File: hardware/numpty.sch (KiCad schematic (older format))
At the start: 46 parts, among them U2 MP3202

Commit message: Rev_0 schematic finished, first pass at PCB layout (no traces yet).
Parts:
- added C1: 4.7uF, Capacitor_SMD:C_1206_3216Metric_Pad1.42x1.75mm_HandSolder, symbol Device:C
- added C2: 2.2uF, Capacitor_SMD:C_1206_3216Metric_Pad1.42x1.75mm_HandSolder, symbol Device:C
- added C3: 10uF, Capacitor_SMD:C_1206_3216Metric_Pad1.42x1.75mm_HandSolder, symbol Device:C
- added C4, C5: 22pF, Capacitor_SMD:C_1206_3216Metric_Pad1.42x1.75mm_HandSolder, symbol Device:C
- added C6: 1uF, Capacitor_SMD:C_1206_3216Metric_Pad1.42x1.75mm_HandSolder, symbol Device:C
- added D1: 30V_500mA_Schottky, Diode_SMD:D_SOD-123, symbol Device:D_Schottky
- added J2: AVR-ISP, Connector_IDC:IDC-Header_2x03_P2.54mm_Vertical, symbol Connector:AVR-ISP-6
- added L1: 10uH, numpty:SRN3010TA, symbol Device:L
- added R1: 100k, Resistor_SMD:R_1206_3216Metric_Pad1.42x1.75mm_HandSolder, symbol Device:R
- added R2: 1.8, Resistor_SMD:R_1206_3216Metric_Pad1.42x1.75mm_HandSolder, symbol Device:R
- added R3, R4: 5k1, Resistor_SMD:R_1206_3216Metric_Pad1.42x1.75mm_HandSolder, symbol Device:R
- added R5, R6: 22, Resistor_SMD:R_1206_3216Metric_Pad1.42x1.75mm_HandSolder, symbol Device:R
- added R7: 10k, Resistor_SMD:R_1206_3216Metric_Pad1.42x1.75mm_HandSolder, symbol Device:R
- added R8: 300, Resistor_SMD:R_1206_3216Metric_Pad1.42x1.75mm_HandSolder, symbol Device:R
- added Y1: 16MHz, Crystal:Crystal_SMD_HC49-SD, symbol Device:Crystal
- D_0, D_1, D_2, D_3, D_4, D_5, D_6, D_7, D_8, D_9, D_M0, D_M1, D_M2, D_M3: footprint (none) -> Diode_SMD:D_SOD-123
- D_DIV0: renamed from D_/; footprint (none) -> Diode_SMD:D_SOD-123
- D_ENT0: renamed from D_ENT; footprint (none) -> Diode_SMD:D_SOD-123
- D_MIN0: renamed from D_-; footprint (none) -> Diode_SMD:D_SOD-123
- D_MUL0: renamed from D_*; footprint (none) -> Diode_SMD:D_SOD-123
- D_NL0: renamed from D_NL; footprint (none) -> Diode_SMD:D_SOD-123
- D_PER0: renamed from D_.; footprint (none) -> Diode_SMD:D_SOD-123
- D_PLU0: renamed from D_+; footprint (none) -> Diode_SMD:D_SOD-123
- J1: renamed from J?; footprint (none) -> Connector_USB:USB_C_Receptacle_GCT_USB4085
- LED_NUMLOCK0: renamed from D_NL_I; footprint (none) -> LED_SMD:LED_Cree-XQ_HandSoldering
- SW_0, SW_1, SW_2, SW_3, SW_4, SW_5, SW_6, SW_7, SW_8, SW_9, SW_M0, SW_M1, SW_M2, SW_M3: footprint (none) -> numpty:Gateron_LED_1.00u_Plate
- SW_DIV0: renamed from SW_/; footprint (none) -> numpty:Gateron_LED_1.00u_Plate
- SW_ENT0: renamed from SW_ENT; footprint (none) -> numpty:Gateron_LED_1.00u_Plate
- SW_MIN0: renamed from SW_-; footprint (none) -> numpty:Gateron_LED_1.00u_Plate
- SW_MUL0: renamed from SW_*; footprint (none) -> numpty:Gateron_LED_1.00u_Plate
- SW_NL0: renamed from SW_NL; footprint (none) -> numpty:Gateron_LED_1.00u_Plate
- SW_PER0: renamed from SW_.; footprint (none) -> numpty:Gateron_LED_1.00u_Plate
- SW_PLU0: renamed from SW_+; footprint (none) -> numpty:Gateron_LED_1.00u_Plate
- U2: footprint (none) -> Package_TO_SOT_SMD:TSOT-23-6_HandSoldering
- gave numbers to parts that had none: 1
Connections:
- net COL0: now also U1.41 (PF0)
- net COL1: now also U1.40 (PF1)
- net COL2: now also U1.39 (PF4)
- net COL3: now also U1.38 (PF5)
- net LEDS_ANODE: now also U2.5 (OV), C2.1, D1.1 (K)
- net LEDS_CATHODE: now also U2.3 (FB), R2.1
- net ROW0: now also U1.18 (PD0)
- net ROW1: now also U1.19 (PD1)
- net ROW2: now also U1.20 (PD2)
- net ROW3: now also U1.21 (PD3)
- net ROW4: now also U1.25 (PD4)
- net ROW5: now also U1.22 (PD5)
- net GND: now reaches J1.A1 (GND)
- net GND: now also J1.A12 (GND), J1.B1 (GND), J1.B12 (GND), LED_NUMLOCK0.2 (A), U1.15 (GND), U1.23 (GND), U1.35 (GND), U1.43 (GND), U1.5 (UGND), U2.2 (GND), C1.2, C2.2, C3.2, C4.2, C5.2, C6.1, J2.6 (GND), R1.2, R2.2, R3.1, R4.1
- net +5V: now reaches J1.A4 (VBUS)
- net +5V: now also J1.A9 (VBUS), J1.B4 (VBUS), J1.B9 (VBUS), U1.14 (VCC), U1.2 (UVCC), U1.24 (AVCC), U1.34 (VCC), U1.44 (AVCC), U1.7 (VBUS), U2.6 (IN), C1.1, C3.1, J2.2 (VCC), L1.1, R7.1
- net at J1.A5 (CC1): now also R3.2
- net at J1.A6 (D+): now also J1.B6 (D+), R6.2
- net at J1.A7 (D-): now also J1.B7 (D-), R5.2
- net at J1.B5 (CC2): now also R4.2
- net at U2.1 (SW): now also D1.2 (A), L1.2
- net LEDS_PWM: now reaches U2.4 (EN)
- net LEDS_PWM: now also U1.32 (PC7), R1.1
- net MOSI: now reaches U1.10 (PB2)
- net MOSI: now also J2.4 (MOSI)
- net MISO: now reaches U1.11 (PB3)
- net MISO: now also J2.1 (MISO)
- net !RESET: now reaches U1.13 (~RESET)
- net !RESET: now also J2.5 (~RST), R7.2
- net at U1.16 (XTAL2): now also C5.1, Y1.2
- net at U1.17 (XTAL1): now also C4.1, Y1.1
- net D-: now reaches U1.3 (D-)
- net D-: now also R5.1
- net at U1.31 (PC6): now also R8.2
- net D+: now reaches U1.4 (D+)
- net D+: now also R6.1
- net at U1.6 (UCAP): now also C6.2
- net SCK: now reaches U1.9 (PB1)
- net SCK: now also J2.3 (SCK)
- net at LED_NUMLOCK0.1 (K): now also R8.1
- no-connect marks 0 -> 15
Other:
- note added: "20210308"
- note added: "numpty"
- moved on the sheet: D_0, D_1, D_2, D_3, D_4, D_5, D_6, D_7, D_8, D_9, D_DIV0, D_ENT0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

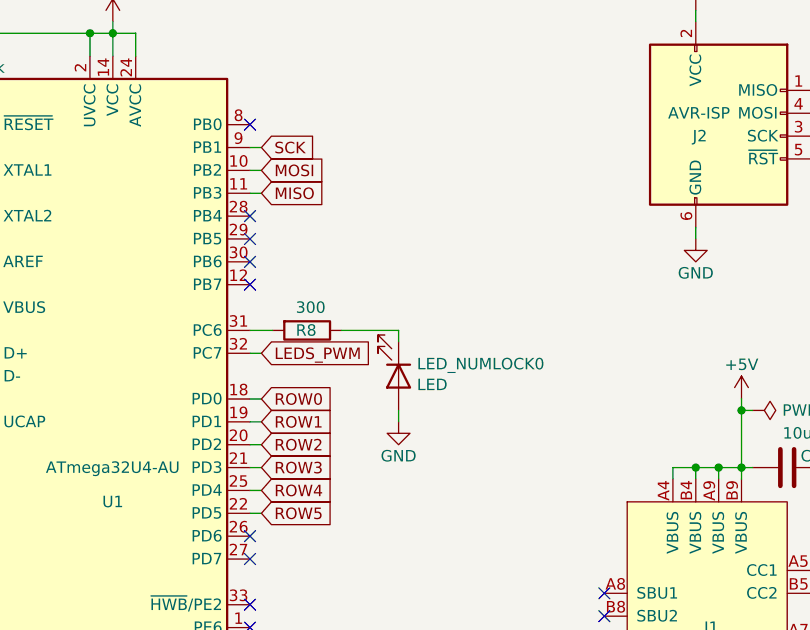
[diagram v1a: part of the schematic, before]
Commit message: Moved led pins to port B.  Added push-button on port B.  Reworked layout to suit these changes.
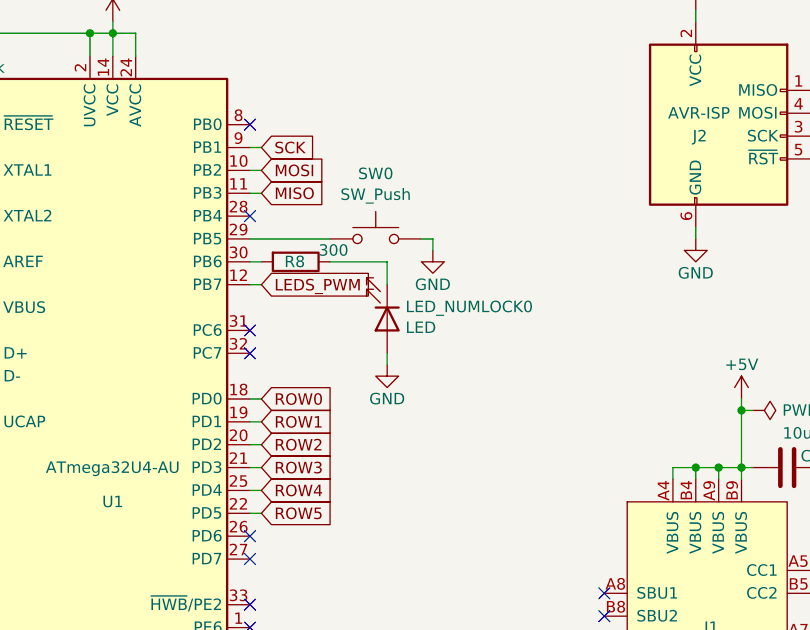
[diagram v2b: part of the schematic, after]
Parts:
- added SW0: SW_Push, Button_Switch_SMD:SW_Push_1P1T_NO_6x6mm_H9.5mm, symbol Switch:SW_Push
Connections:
- net GND: now also SW0.2
- net LEDS_PWM: now also U1.12 (PB7); no longer U1.32 (PC7)
- net at U1.29 (PB5): now also SW0.1
- net at U1.30 (PB6): now also R8.2
- net at U1.31 (PC6): no longer R8.2
- no-connect marks 15 -> 14
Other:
- moved on the sheet: LED_NUMLOCK0, R8
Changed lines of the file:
@@
 L Device:LED LED_NUMLOCK0
 U 1 1 60849E17
-P 8050 2450
-F 0 "LED_NUMLOCK0" V 7997 2530 50  0000 L CNN
-F 1 "LED" V 8088 2530 50  0000 L CNN
-F 2 "LED_SMD:LED_Cree-XQ_HandSoldering" H 8050 2450 50  0001 C CNN
-F 3 "~" H 8050 2450 50  0001 C CNN
-	1    8050 2450
+P 8000 2200
+F 0 "LED_NUMLOCK0" V 7947 2280 50  0000 L CNN
+F 1 "LED" V 8038 2280 50  0000 L CNN
+F 2 "LED_SMD:LED_Cree-XQ_HandSoldering" H 8000 2200 50  0001 C CNN
+F 3 "~" H 8000 2200 50  0001 C CNN
+	1    8000 2200
 	0    1    1    0
 $EndComp
@@
 L Device:R R8
 U 1 1 60C3E138
-P 7650 2250
-F 0 "R8" V 7650 2200 50  0000 L CNN
-F 1 "300" V 7550 2200 50  0000 L CNN
-F 2 "Resistor_SMD:R_1206_3216Metric_Pad1.42x1.75mm_HandSolder" V 7580 2250 50  0001 C CNN
-F 3 "~" H 7650 2250 50  0001 C CNN
-	1    7650 2250
+P 7600 1950
+F 0 "R8" V 7600 1900 50  0000 L CNN
+F 1 "300" V 7550 2050 50  0000 L CNN
+F 2 "Resistor_SMD:R_1206_3216Metric_Pad1.42x1.75mm_HandSolder" V 7530 1950 50  0001 C CNN
+F 3 "~" H 7600 1950 50  0001 C CNN
+	1    7600 1950
 	0    1    1    0
 $EndComp
@@
 Wire Wire Line
 	9350 900  9350 850
-Text GLabel 7450 2350 2    50   Input ~ 0
+Text GLabel 7450 2050 2    50   Input ~ 0
 LEDS_PWM
 Text GLabel 7450 2550 2    50   Input ~ 0
@@
 Text GLabel 7450 4050 2    50   Input ~ 0
 COL3
-Wire Wire Line
-	7400 2250 7500 2250
-Wire Wire Line
-	7800 2250 8050 2250
-Wire Wire Line
-	8050 2250 8050 2300
 $Comp
 L power:GND #PWR0115
 U 1 1 60F7D3CB
-P 8050 2650
-F 0 "#PWR0115" H 8050 2400 50  0001 C CNN
-F 1 "GND" H 8050 2500 50  0000 C CNN
-F 2 "" H 8050 2650 50  0001 C CNN
-F 3 "" H 8050 2650 50  0001 C CNN
-	1    8050 2650
-	1    0    0    -1
-$EndComp
-Wire Wire Line
-	8050 2650 8050 2600
-Wire Wire Line
-	7450 2350 7400 2350
+P 8000 2400
+F 0 "#PWR0115" H 8000 2150 50  0001 C CNN
+F 1 "GND" H 8000 2250 50  0000 C CNN
+F 2 "" H 8000 2400 50  0001 C CNN
+F 3 "" H 8000 2400 50  0001 C CNN
+	1    8000 2400
+	1    0    0    -1
+$EndComp
 Wire Wire Line
 	7400 2550 7450 2550
@@
 NoConn ~ 7400 1750
 NoConn ~ 7400 1350
-NoConn ~ 7400 1850
-NoConn ~ 7400 1950
-NoConn ~ 7400 2050
 NoConn ~ 7400 3150
 NoConn ~ 7400 3250
@@
 	1    0    0    -1
 $EndComp
+Wire Wire Line
+	7450 1950 7400 1950
+Wire Wire Line
+	7400 2050 7450 2050
+Wire Wire Line
+	8000 1950 7750 1950
+NoConn ~ 7400 2350
+NoConn ~ 7400 2250
+$Comp
+L Switch:SW_Push SW0
+U 1 1 605D1A0D
+P 7950 1850
+F 0 "SW0" H 7950 2135 50  0000 C CNN
+F 1 "SW_Push" H 7950 2044 50  0000 C CNN
+F 2 "Button_Switch_SMD:SW_Push_1P1T_NO_6x6mm_H9.5mm" H 7950 2050 50  0001 C CNN
+F 3 "~" H 7950 2050 50  0001 C CNN
+	1    7950 1850
+	1    0    0    -1
+$EndComp
+Wire Wire Line
+	7400 1850 7750 1850
+$Comp
+L power:GND #PWR0116
+U 1 1 605EDB5F
+P 8200 1900
+F 0 "#PWR0116" H 8200 1650 50  0001 C CNN
+F 1 "GND" H 8200 1750 50  0000 C CNN
+F 2 "" H 8200 1900 50  0001 C CNN
+F 3 "" H 8200 1900 50  0001 C CNN
+	1    8200 1900
+	1    0    0    -1
+$EndComp
+Wire Wire Line
+	8150 1850 8200 1850
+Wire Wire Line
+	8200 1850 8200 1900
+Wire Wire Line
+	8000 1950 8000 2050
+Wire Wire Line
+	8000 2350 8000 2400
 $EndSCHEMATC

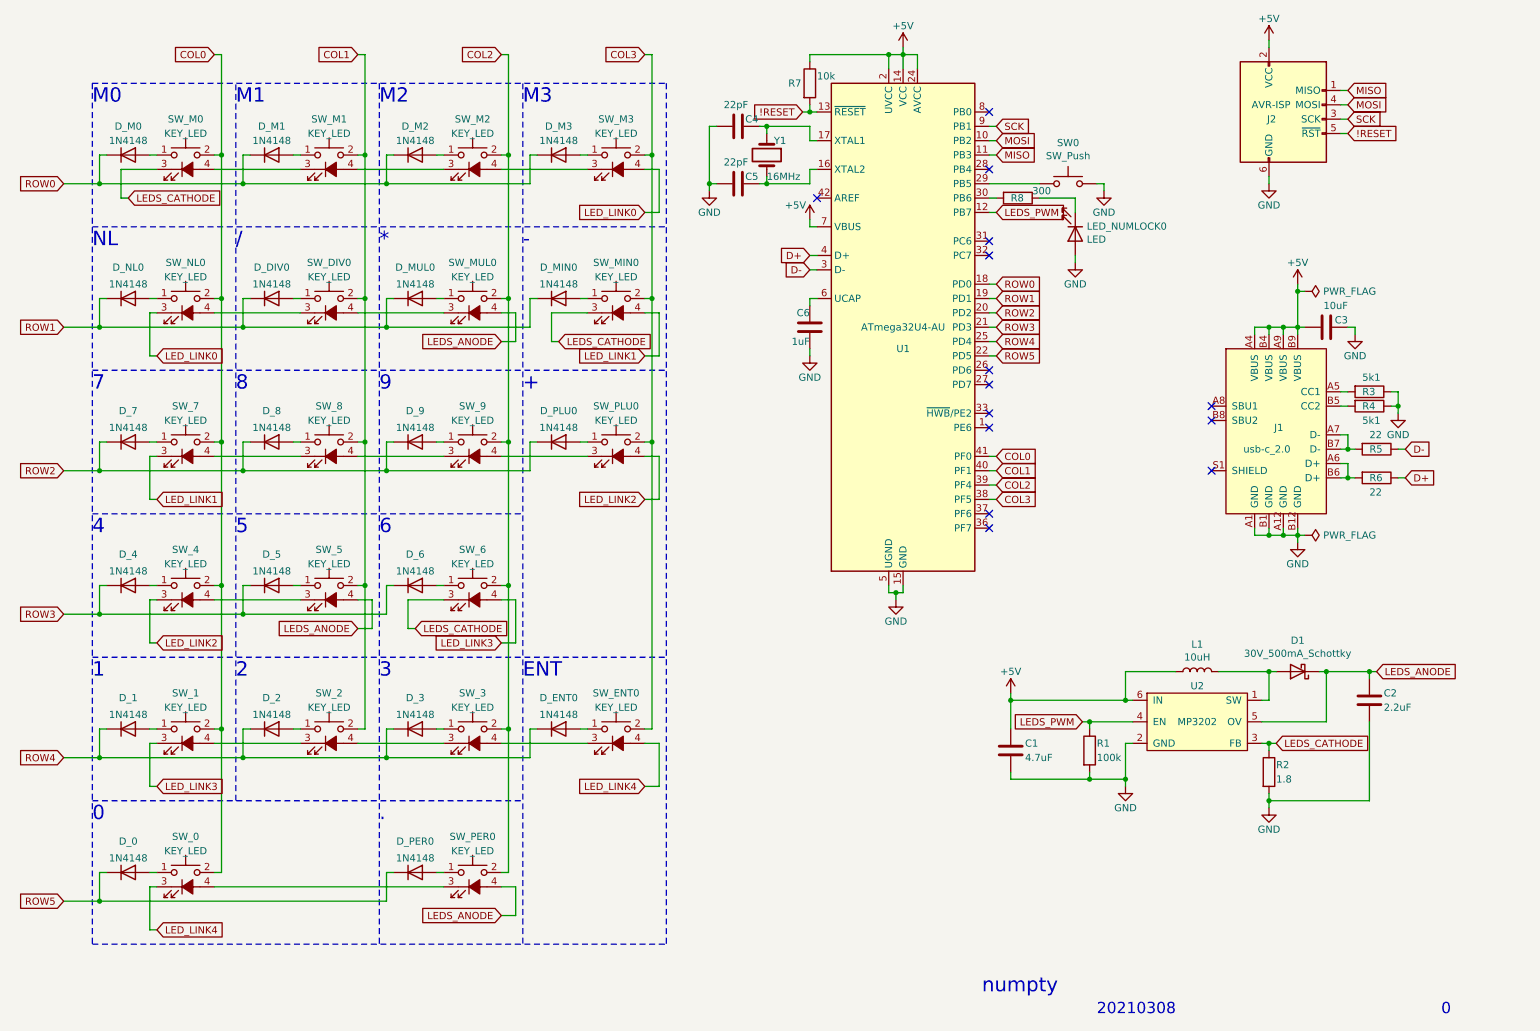
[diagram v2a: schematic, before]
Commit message: Cleaned up rev 0 PCB layout, ordered fabrication.  Added .gitignore.
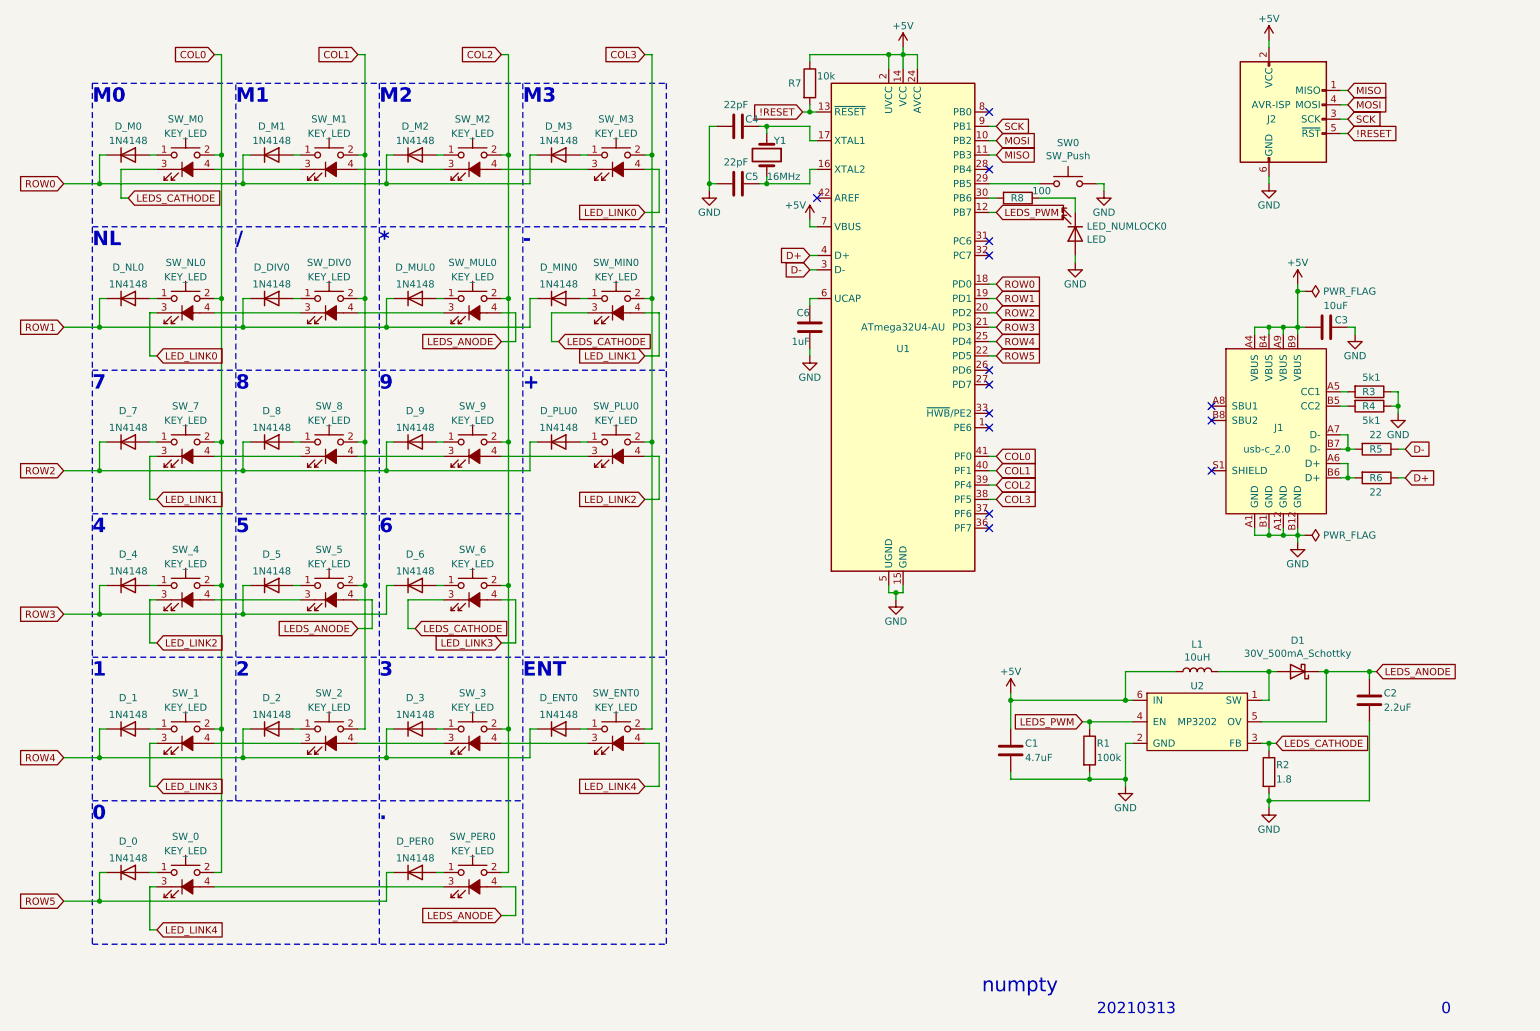
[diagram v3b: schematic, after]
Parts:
- R8: value 300 -> 100
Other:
- note added: "20210313"
- note removed: "20210308"
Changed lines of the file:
@@
 	1    0    0    -1
 $EndComp
-Wire Notes Line
+Wire Notes Line width 20
 	1150 1150 5150 1150
-Wire Notes Line
+Wire Notes Line width 20
 	1150 2150 5150 2150
-Wire Notes Line
+Wire Notes Line width 20
 	1150 3150 5150 3150
-Wire Notes Line
+Wire Notes Line width 20
 	1150 5150 5150 5150
-Wire Notes Line
+Wire Notes Line width 20
 	1150 7150 5150 7150
-Wire Notes Line
+Wire Notes Line width 20
 	4150 1150 4150 7150
-Wire Notes Line
+Wire Notes Line width 20
 	3150 1150 3150 7150
-Wire Notes Line
+Wire Notes Line width 20
 	1150 1150 1150 7150
-Wire Notes Line
+Wire Notes Line width 20
 	5150 1150 5150 7150
-Wire Notes Line
+Wire Notes Line width 20
 	2150 6150 2150 1150
-Wire Notes Line
+Wire Notes Line width 20
 	1150 6150 4150 6150
-Wire Notes Line
+Wire Notes Line width 20
 	1150 4150 4150 4150
-Text Notes 1150 1300 0    100  ~ 0
+Text Notes 1150 1300 0    100  ~ 20
 M0
-Text Notes 2150 1300 0    100  ~ 0
+Text Notes 2150 1300 0    100  ~ 20
 M1
-Text Notes 3150 1300 0    100  ~ 0
+Text Notes 3150 1300 0    100  ~ 20
 M2
-Text Notes 4150 1300 0    100  ~ 0
+Text Notes 4150 1300 0    100  ~ 20
 M3
 Wire Wire Line
@@
 Wire Wire Line
 	5100 2750 5000 2750
-Text Notes 1150 2300 0    100  ~ 0
+Text Notes 1150 2300 0    100  ~ 20
 NL
-Text Notes 2150 2300 0    100  ~ 0
+Text Notes 2150 2300 0    100  ~ 20
 /
-Text Notes 3150 2300 0    100  ~ 0
+Text Notes 3150 2300 0    100  ~ 20
 *
-Text Notes 4150 2300 0    100  ~ 0
+Text Notes 4150 2300 0    100  ~ 20
 -
-Text Notes 4150 3300 0    100  ~ 0
+Text Notes 4150 3300 0    100  ~ 20
 +
-Text Notes 3150 3300 0    100  ~ 0
+Text Notes 3150 3300 0    100  ~ 20
 9
-Text Notes 2150 3300 0    100  ~ 0
+Text Notes 2150 3300 0    100  ~ 20
 8
-Text Notes 1150 3300 0    100  ~ 0
+Text Notes 1150 3300 0    100  ~ 20
 7
-Text Notes 1150 4300 0    100  ~ 0
+Text Notes 1150 4300 0    100  ~ 20
 4
-Text Notes 2150 4300 0    100  ~ 0
+Text Notes 2150 4300 0    100  ~ 20
 5
-Text Notes 3150 4300 0    100  ~ 0
+Text Notes 3150 4300 0    100  ~ 20
 6
-Text Notes 1150 5300 0    100  ~ 0
+Text Notes 1150 5300 0    100  ~ 20
 1
-Text Notes 2150 5300 0    100  ~ 0
+Text Notes 2150 5300 0    100  ~ 20
 2
-Text Notes 3150 5300 0    100  ~ 0
+Text Notes 3150 5300 0    100  ~ 20
 3
-Text Notes 4150 5300 0    100  ~ 0
+Text Notes 4150 5300 0    100  ~ 20
 ENT
-Text Notes 1150 6300 0    100  ~ 0
+Text Notes 1150 6300 0    100  ~ 20
 0
-Text Notes 3150 6300 0    100  ~ 0
+Text Notes 3150 6300 0    100  ~ 20
 .
 $Comp
@@
 P 7600 1950
 F 0 "R8" V 7600 1900 50  0000 L CNN
-F 1 "300" V 7550 2050 50  0000 L CNN
+F 1 "100" V 7550 2050 50  0000 L CNN
 F 2 "Resistor_SMD:R_1206_3216Metric_Pad1.42x1.75mm_HandSolder" V 7530 1950 50  0001 C CNN
 F 3 "~" H 7600 1950 50  0001 C CNN
@@
 numpty
 Text Notes 8150 7650 0    79   ~ 0
-20210308
+20210313
 Text Notes 10550 7650 0    79   ~ 0
 0
